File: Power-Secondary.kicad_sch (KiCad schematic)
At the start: 34 parts, among them J1 PowerConn, J2 PowerConn, J3 PowerConn, J4 PowerConn, J5 Conn_01x03, Q1 SQJQ140E-T1_GE3, Q2 SQJQ140E-T1_GE3, Q3 SQJQ140E-T1_GE3, Q4 SQJQ140E-T1_GE3, Q5 SQJ141ELP, Q6 NMOS, Q7 PMOS, U1 TLV9061QDCKRQ1

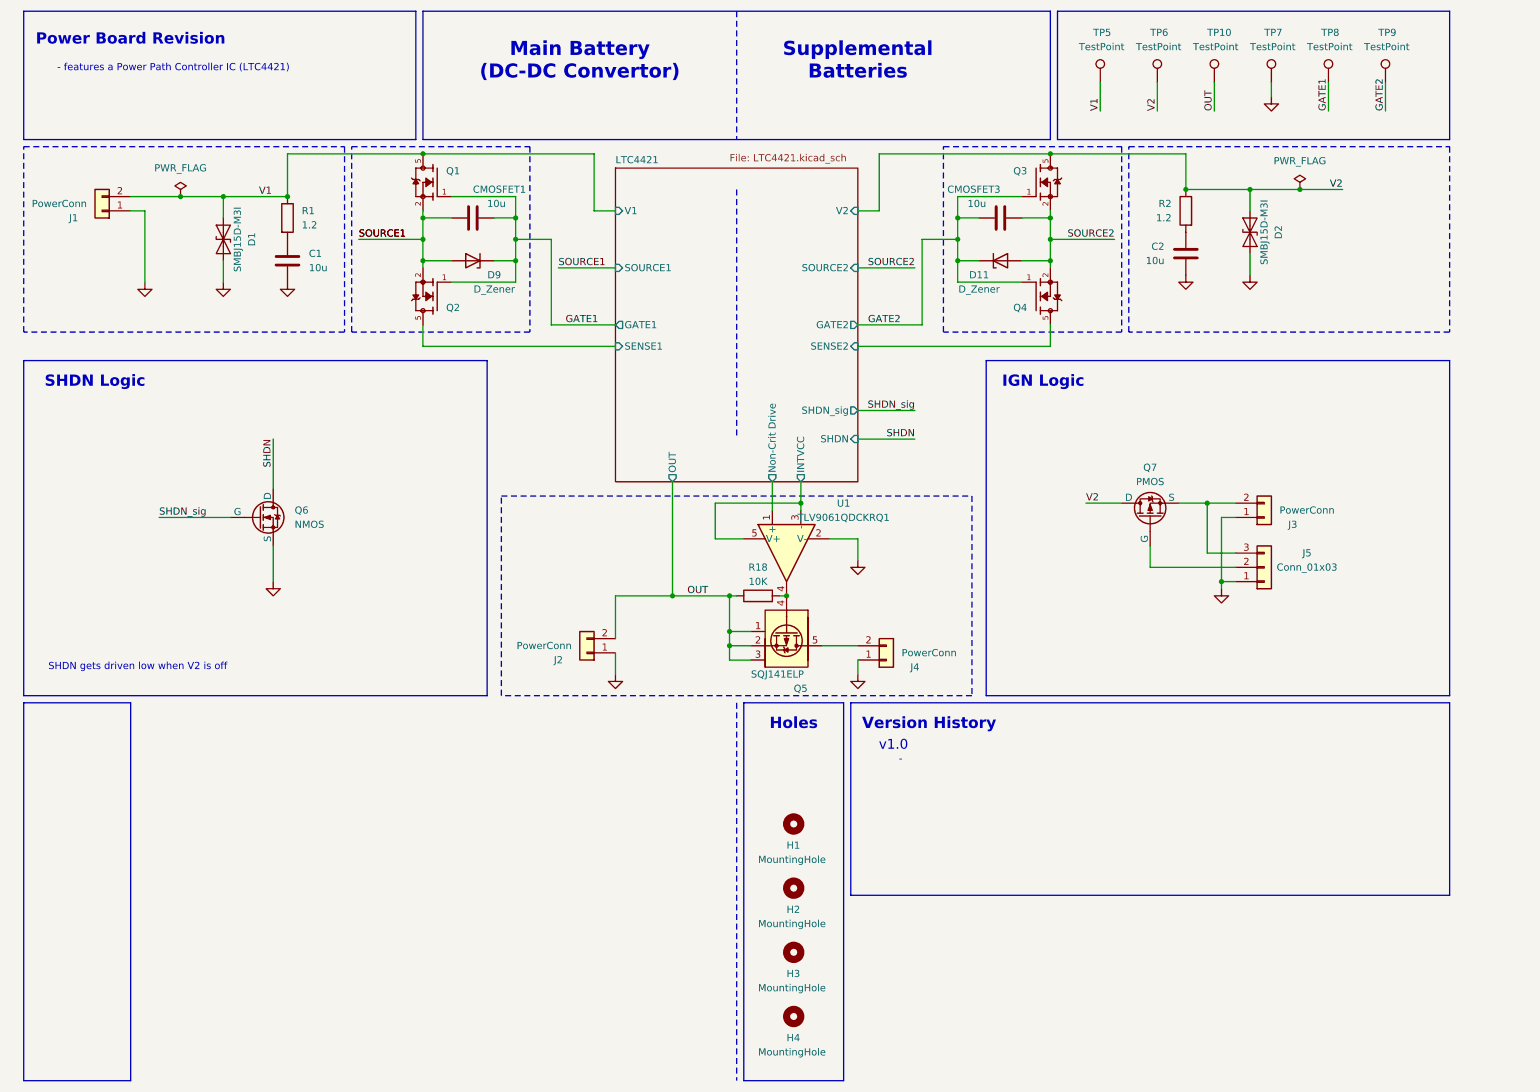
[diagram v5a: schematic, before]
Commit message: add high side switch schematic
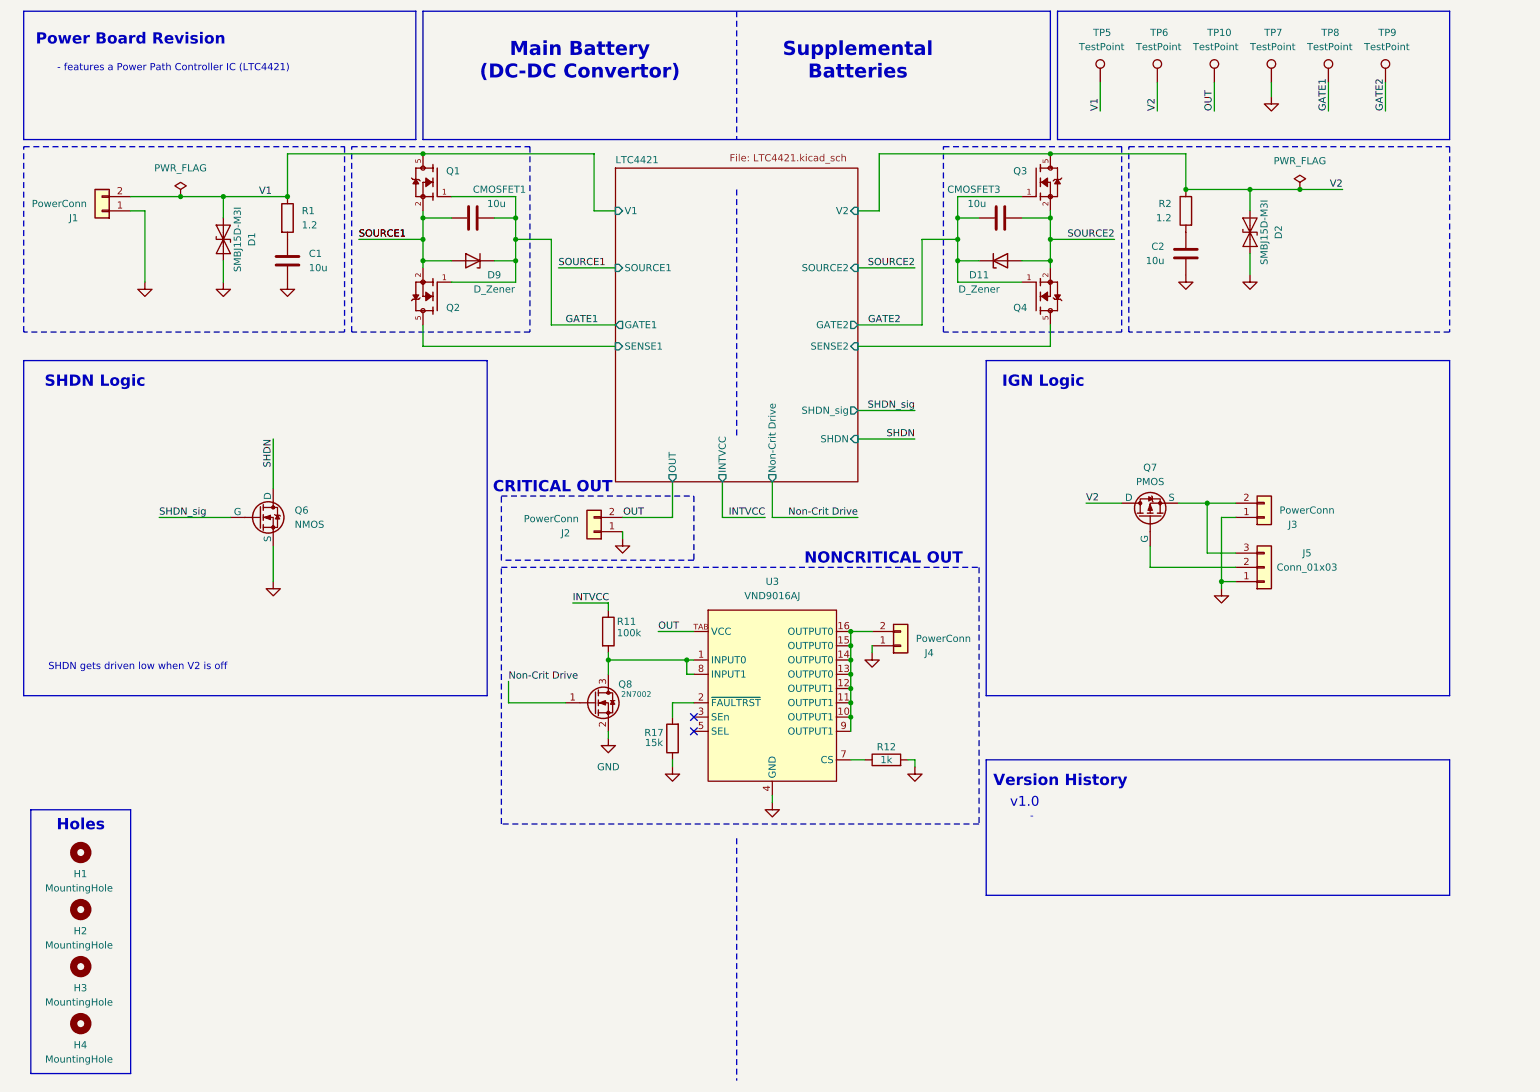
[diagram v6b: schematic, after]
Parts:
- removed Q5: SQJ141ELP, Package_SO:PowerPAK_SO-8L_Single, symbol PowerBoardLib:SQJ141ELP
- removed R18: 10K, Resistor_SMD:R_0805_2012Metric, symbol Device:R
- removed U1: TLV9061QDCKRQ1, Package_TO_SOT_SMD:SOT-353_SC-70-5, symbol Comparator:LM397
- added Q8: 2N7002, Package_TO_SOT_SMD:SOT-23, symbol Transistor_FET:Q_NMOS_GSD
- added R11: 100k, Resistor_SMD:R_0805_2012Metric, symbol Device:R
- added R12: 1k, Resistor_SMD:R_0805_2012Metric, symbol Device:R
- added R17: 15k, Resistor_SMD:R_0805_2012Metric, symbol Device:R
- added U3: VND9016AJ, Package_SO:PowerSSO-16-1EP_3.9x4.9mm_P0.5mm_EP2.5x3.61mm, symbol PowerBoardLib:VN9016AJ
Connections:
- net GND: now also Q8.2 (S), R12.2, R17.1, U3.4 (GND)
- net OUT: now also U3.TAB (VCC)
- net at J4.2 (Pin_2): now also U3.10 (OUTPUT1), U3.11 (OUTPUT1), U3.12 (OUTPUT1), U3.13 (OUTPUT0), U3.14 (OUTPUT0), U3.15 (OUTPUT0), U3.16 (OUTPUT0), U3.9 (OUTPUT1)
- new net: Q8.3 (D), R11.2, U3.1 (INPUT0), U3.8 (INPUT1)
- new net: R17.2, U3.2 (~{FAULTRST})
- new net: R12.1, U3.7 (CS)
- new net INTVCC: R11.1
- new net Non-Crit Drive: Q8.1 (G)
- no-connect marks 0 -> 2
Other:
- note added: "CRITICAL OUT"
- note added: "NONCRITICAL OUT"
- moved on the sheet: H1, H2, H3, H4, J2, J4

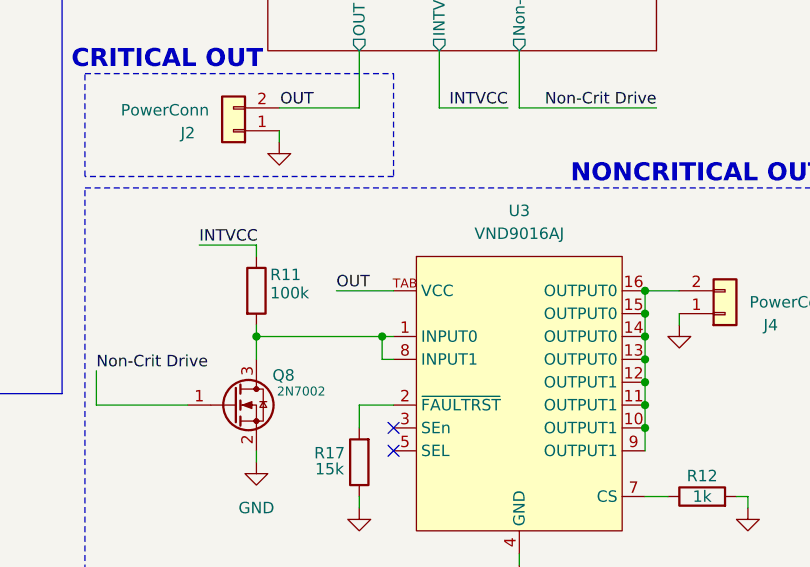
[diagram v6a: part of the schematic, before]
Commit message: Non-crit layout
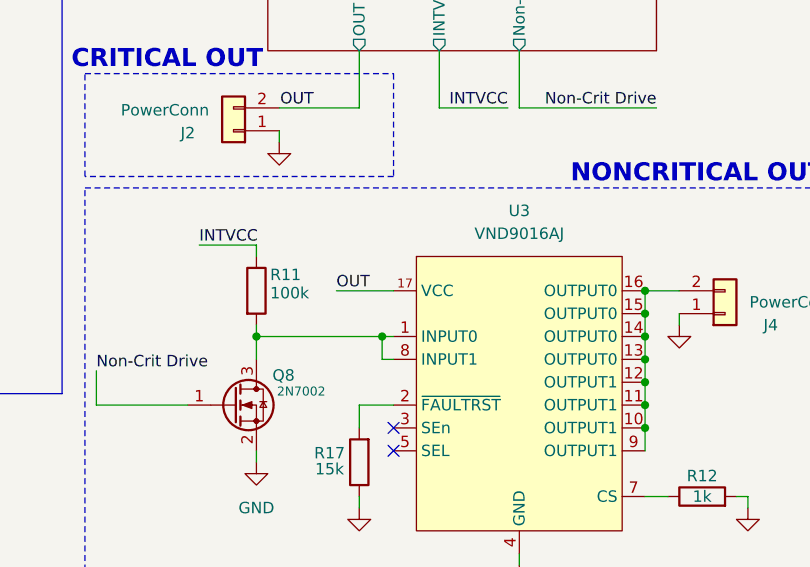
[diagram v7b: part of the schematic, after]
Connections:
- net OUT: now also U3.17 (VCC); no longer U3.TAB (VCC)
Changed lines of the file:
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@@
 			)
 		)
-		(pin "TAB"
+		(pin "17"
 		)
 		(pin "8"

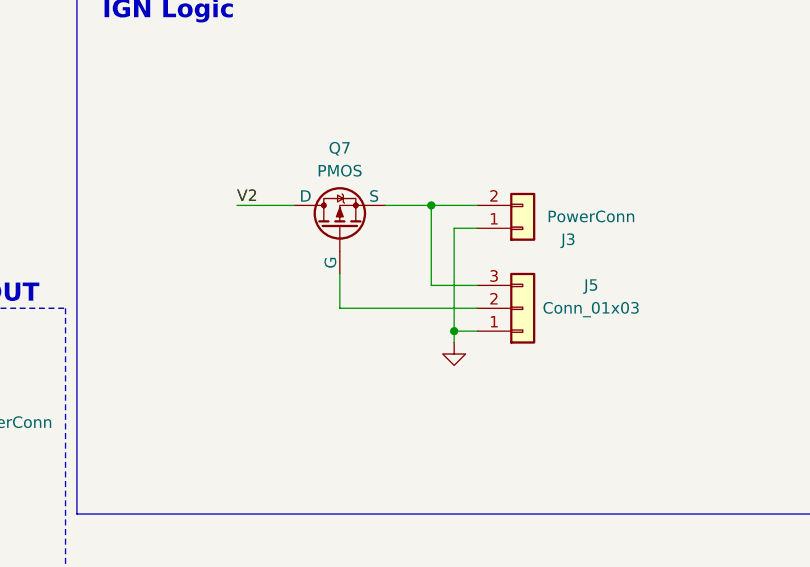
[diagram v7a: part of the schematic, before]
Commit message: changed UV and OV resistor circuit
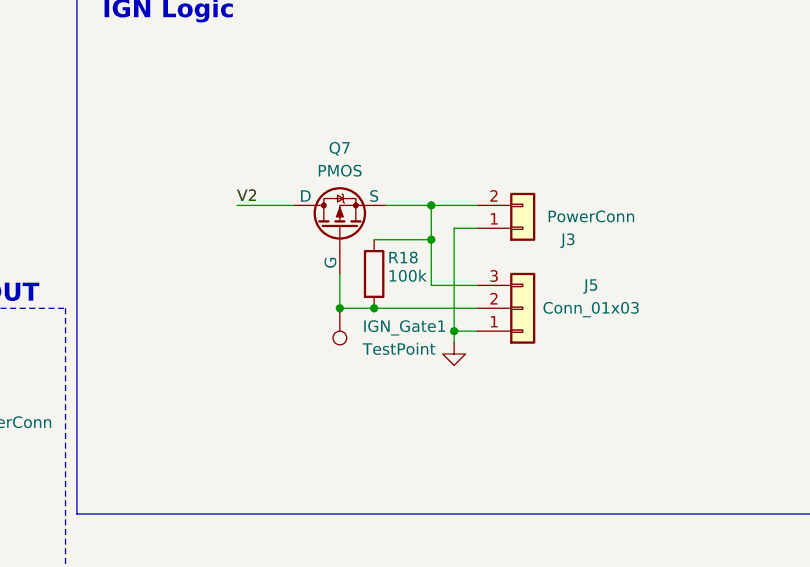
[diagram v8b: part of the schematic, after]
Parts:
- added IGN_Gate1: TestPoint, TestPoint:TestPoint_Pad_D2.0mm, symbol Connector:TestPoint
- added R18: 100k, Resistor_SMD:R_0805_2012Metric, symbol Device:R
- Q6: footprint Package_TO_SOT_SMD:TSOT-23 -> Package_TO_SOT_SMD:SOT-23
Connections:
- net at J5.2 (Pin_2), Q7.2 (G): now also IGN_Gate1.1, R18.2
- net at J3.2 (Pin_2), J5.3 (Pin_3), Q7.3 (S): now also R18.1
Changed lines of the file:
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@@
 	)
 	(junction
+		(at 213.36 111.76)
+		(diameter 0)
+		(color 0 0 0 0)
+	)
+	(junction
 		(at 160.02 125.73)
 		(diameter 0)
@@
 	)
 	(junction
+		(at 217.17 111.76)
+		(diameter 0)
+		(color 0 0 0 0)
+	)
+	(junction
 		(at 48.26 45.72)
 		(diameter 0)
@@
 	)
 	(junction
+		(at 223.52 104.14)
+		(diameter 0)
+		(color 0 0 0 0)
+	)
+	(junction
 		(at 100.33 57.15)
 		(diameter 0)
@@
 	(wire
 		(pts
+			(xy 217.17 111.76) (xy 228.6 111.76)
+		)
+		(stroke
+			(width 0)
+			(type default)
+		)
+	)
+	(wire
+		(pts
 			(xy 48.26 45.72) (xy 59.69 45.72)
 		)
@@
 	(wire
 		(pts
+			(xy 223.52 104.14) (xy 223.52 100.33)
+		)
+		(stroke
+			(width 0)
+			(type default)
+		)
+	)
+	(wire
+		(pts
 			(xy 161.29 72.39) (xy 195.58 72.39)
 		)
@@
 	(wire
 		(pts
+			(xy 217.17 104.14) (xy 223.52 104.14)
+		)
+		(stroke
+			(width 0)
+			(type default)
+		)
+	)
+	(wire
+		(pts
 			(xy 100.33 45.72) (xy 100.33 49.53)
 		)
@@
 	(wire
 		(pts
-			(xy 223.52 109.22) (xy 223.52 100.33)
+			(xy 223.52 109.22) (xy 223.52 104.14)
 		)
 		(stroke
@@
 	(wire
 		(pts
-			(xy 213.36 111.76) (xy 228.6 111.76)
+			(xy 213.36 111.76) (xy 217.17 111.76)
 		)
 		(stroke
@@
 	)
 	(symbol
+		(lib_id "Connector:TestPoint")
+		(at 213.36 111.76 180)
+		(unit 1)
+		(exclude_from_sim no)
+		(in_bom yes)
+		(on_board yes)
+		(dnp no)
+		(property "Reference" "IGN_Gate1"
+			(at 215.9 113.7919 0)
+			(effects
+				(font
+					(size 1.27 1.27)
+				)
+				(justify right)
+			)
+		)
+		(property "Value" "TestPoint"
+			(at 215.9 116.3319 0)
+			(effects
+				(font
+					(size 1.27 1.27)
+				)
+				(justify right)
+			)
+		)
+		(property "Footprint" "TestPoint:TestPoint_Pad_D2.0mm"
+			(at 208.28 111.76 0)
+			(effects
+				(font
+					(size 1.27 1.27)
+				)
+				(hide yes)
+			)
+		)
+		(property "Datasheet" "~"
+			(at 208.28 111.76 0)
+			(effects
+				(font
+					(size 1.27 1.27)
+				)
+				(hide yes)
+			)
+		)
+		(property "Description" "test point"
+			(at 213.36 111.76 0)
+			(effects
+				(font
+					(size 1.27 1.27)
+				)
+				(hide yes)
+			)
+		)
+		(pin "1"
+		)
+		(instances
+			(project ""
+				(path "/ba21eba1-72a9-489c-9498-a38516b9f252"
+					(reference "IGN_Gate1")
+					(unit 1)
+				)
+			)
+		)
+	)
+	(symbol
 		(lib_id "Simulation_SPICE:NMOS")
 		(at 54.61 102.87 0)
@@
 			)
 		)
-		(property "Footprint" "Package_TO_SOT_SMD:TSOT-23"
+		(property "Footprint" "Package_TO_SOT_SMD:SOT-23"
 			(at 59.69 100.33 0)
 			(effects
@@
 					(unit 1)
 				)
+			)
+		)
+	)
+	(symbol
+		(lib_id "Device:R")
+		(at 217.17 107.95 0)
+		(unit 1)
+		(exclude_from_sim no)
+		(in_bom yes)
+		(on_board yes)
+		(dnp no)
+		(property "Reference" "R18"
+			(at 218.694 106.172 0)
+			(effects
+				(font
+					(size 1.27 1.27)
+				)
+				(justify left)
+			)
+		)
+		(property "Value" "100k"
+			(at 218.694 108.204 0)
+			(effects
+				(font
+					(size 1.27 1.27)
+				)
+				(justify left)
+			)
+		)
+		(property "Footprint" "Resistor_SMD:R_0805_2012Metric"
+			(at 215.392 107.95 90)
+			(effects
+				(font
+					(size 1.27 1.27)
+				)
+				(hide yes)
+			)
+		)
+		(property "Datasheet" "~"
+			(at 217.17 107.95 0)
+			(effects
+				(font
+					(size 1.27 1.27)
+				)
+				(hide yes)
+			)
+		)
+		(property "Description" "Resistor"
+			(at 217.17 107.95 0)
+			(effects
+				(font
+					(size 1.27 1.27)
+				)
+				(hide yes)
+			)
+		)
+		(pin "1"
+		)
+		(pin "2"
+		)
+		(instances
+			(project "Power-Secondary"
+				(path "/ba21eba1-72a9-489c-9498-a38516b9f252"
+					(reference "R18")
+					(unit 1)
+				)
